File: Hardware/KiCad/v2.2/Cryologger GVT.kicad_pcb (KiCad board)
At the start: 2 copper layers, 144.1 x 96.5 mm, 14 parts, among them J1 Screw_Terminal_01x02, U1 SparkFun_MMDLCB, U2 SparkFun_ZED-F9P, U3 Pololu_D36V6x

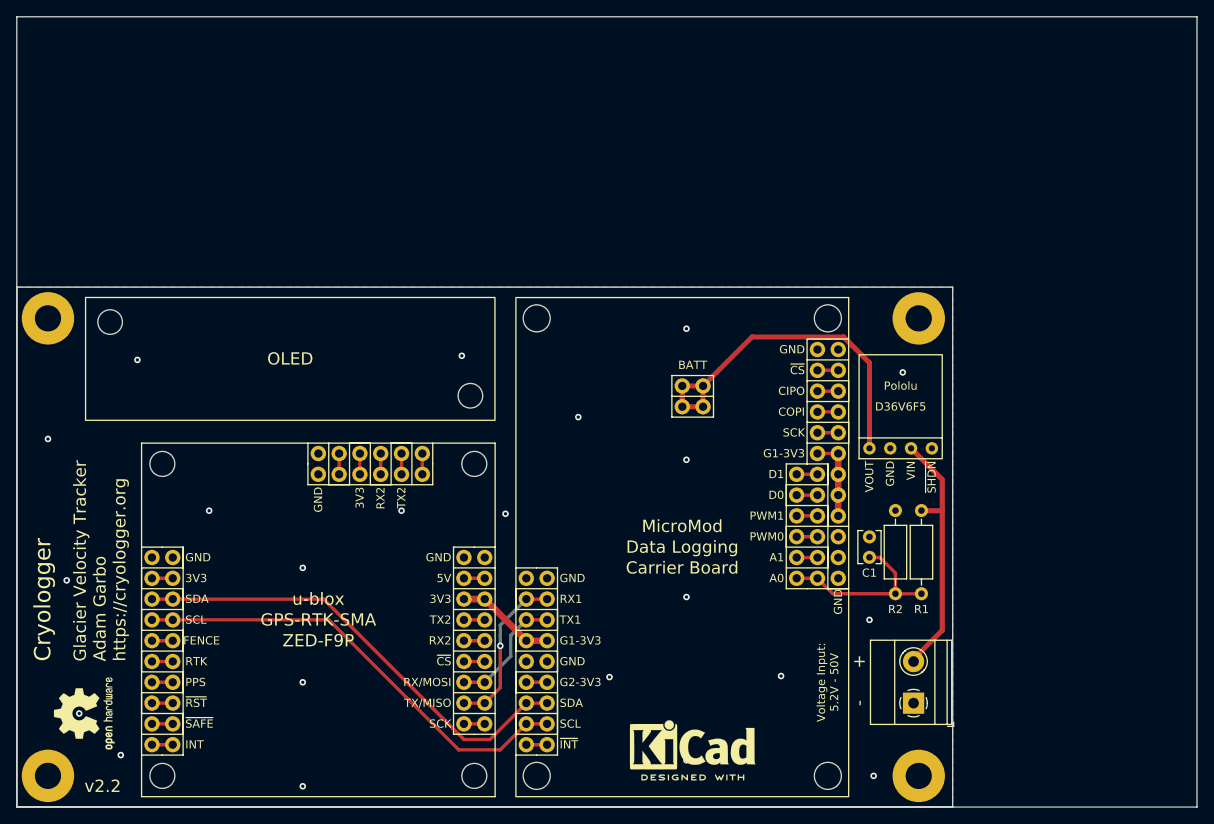
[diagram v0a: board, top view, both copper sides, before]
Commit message: Fix orientation of PCB OLED mounting holes
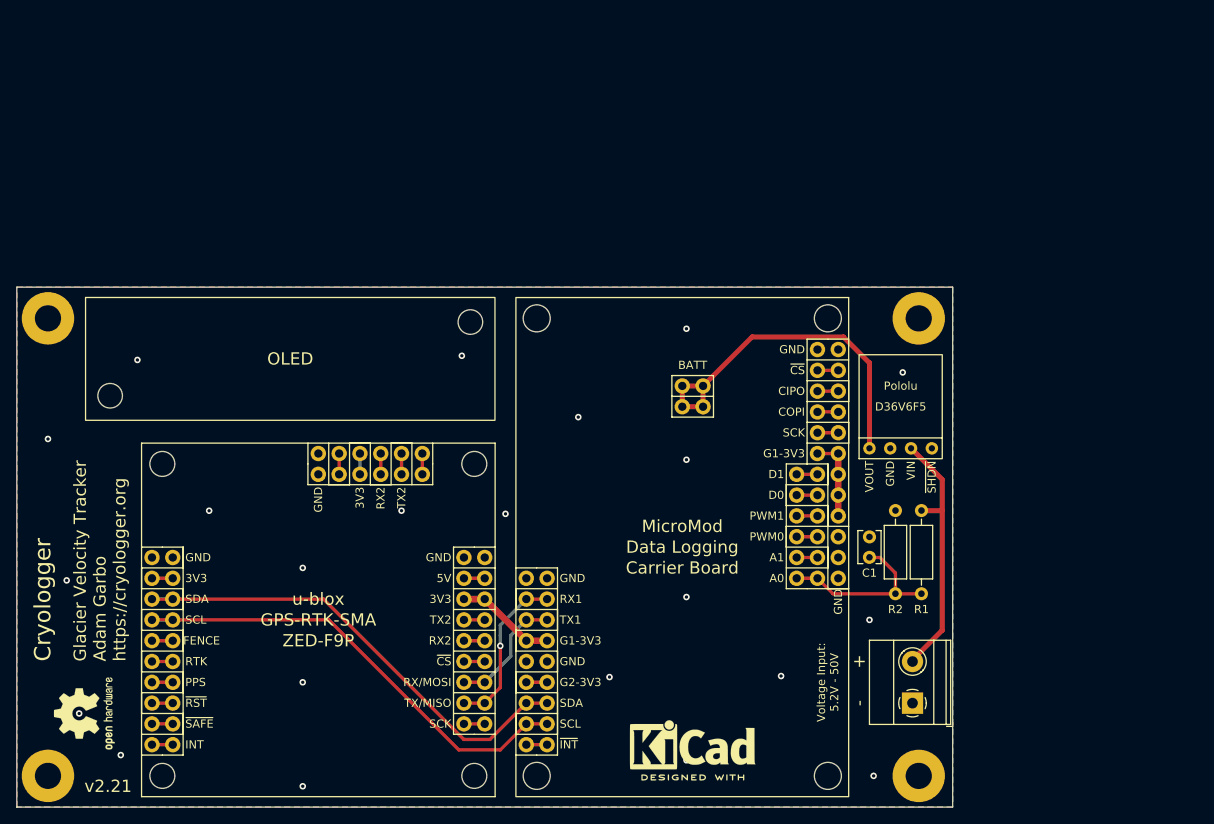
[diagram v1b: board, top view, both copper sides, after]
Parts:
- moved J1 0.13 mm to (200.8, 113.0)
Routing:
- net SDA: track 57.2 -> 59.7 mm
- net SCL: track 56.2 -> 58.7 mm
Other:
- board size 144.1 x 96.5 mm -> 114.3 x 63.5 mm
- board text added: "v2.21"
- board text removed: "v2.2"
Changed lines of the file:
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@@
     )
   )
-  (footprint "Cryologger:SparkFun_OLED" locked (layer "F.Cu")
+  (footprint "Cryologger:SparkFun_OLED" (layer "F.Cu")
     (at 124.841 70.993)
     (attr through_hole)
@@
       (effects (font (size 1 1) (thickness 0.15)))
     )
-    (fp_text value "SparkFun_OLED" (at 0 8.85 unlocked) (layer "F.Fab")
+    (fp_text value "SparkFun_OLED" (at 0 8.85 unlocked) (layer "F.Fab") hide
       (effects (font (size 1 1) (thickness 0.15)))
     )
+    (fp_text user "SparkFun OLED" (at 0 0 unlocked) (layer "F.SilkS") hide
+      (effects (font (size 1.5 1.5) (thickness 0.3)))
+    )
     (fp_text user "OLED" (at 0 0 unlocked) (layer "F.SilkS")
       (effects (font (size 1.5 1.5) (thickness 0.3)))
@@
     )
     (fp_rect (start -25 -7.5) (end 25 7.5) (layer "F.SilkS") (width 0.12) (fill none))
-    (pad "" np_thru_hole circle locked (at 22 4.5) (size 3 3) (drill 3) (layers F&B.Cu *.Mask))
-    (pad "" np_thru_hole circle locked (at -22 -4.5) (size 3 3) (drill 3) (layers F&B.Cu *.Mask))
+    (pad "" np_thru_hole circle (at 22 -4.5) (size 3 3) (drill 3) (layers F&B.Cu *.Mask))
+    (pad "" np_thru_hole circle (at -22 4.5) (size 3 3) (drill 3) (layers F&B.Cu *.Mask))
   )
   (footprint "MountingHole:MountingHole_3.2mm_M3_Pad" (layer "F.Cu")
@@
   )
   (footprint "TerminalBlock_Phoenix:TerminalBlock_Phoenix_MKDS-1,5-2-5.08_1x02_P5.08mm_Horizontal" (layer "F.Cu")
-    (at 200.965003 113.035004 90)
+    (at 200.838 113.035004 90)
     (descr "Terminal Block Phoenix MKDS-1,5-2-5.08, 2 pins, pitch 5.08mm, size 10.2x9.8mm^2, drill diamater 1.3mm, pad diameter 2.6mm, see http://www.farnell.com/datasheets/100425.pdf, script-generated using https://github.com/pointhi/kicad-footprint-generator/scripts/TerminalBlock_Phoenix")
     (tags "THT Terminal Block Phoenix MKDS-1,5-2-5.08 pitch 5.08mm size 10.2x9.8mm^2 drill 1.3mm pad 2.6mm")
@@
   )
   (gr_rect (start 113.03 99.695) (end 143.51 122.555) (layer "B.SilkS") (width 0.15) (fill solid))
-  (gr_rect (start 91.44 125.73) (end 235.585 29.21) (layer "Edge.Cuts") (width 0.1) (fill none))
   (gr_rect (start 91.44 62.23) (end 205.74 125.73) (layer "Edge.Cuts") (width 0.1) (fill none))
   (gr_text "Notes:" (at 140.335 97.79) (layer "B.SilkS")
@@
     (effects (font (size 1.5 1.5) (thickness 0.3)))
   )
-  (gr_text "v2.2" (at 99.695 123.19) (layer "F.SilkS")
+  (gr_text "v2.21" (at 99.695 123.19) (layer "F.SilkS")
     (effects (font (size 1.5 1.5) (thickness 0.3)) (justify left))
   )
@@
     (pts (xy 91.44 125.73) (xy 91.44 62.23))
     (height -3.81)
-    (gr_text "2.5000 in" (at 86.48 93.98 90) (layer "Dwgs.User")
+    (gr_text "2500.0000 mils" (at 86.48 93.98 90) (layer "Dwgs.User")
       (effects (font (size 1 1) (thickness 0.15)))
     )
@@
     (pts (xy 91.44 125.73) (xy 205.74 125.73))
     (height 3.81)
-    (gr_text "4.5000 in" (at 148.59 128.39) (layer "Dwgs.User")
+    (gr_text "4500.0000 mils" (at 148.59 128.39) (layer "Dwgs.User")
       (effects (font (size 1 1) (thickness 0.15)))
     )
@@
     (style (thickness 0.15) (arrow_length 1.27) (text_position_mode 0) (extension_height 0.58642) (extension_offset 0.5) keep_text_aligned)
   )
-  (dimension (type aligned) (layer "Edge.Cuts")
-    (pts (xy 235.585 125.73) (xy 235.585 29.21))
-    (height 5.08)
-    (gr_text "3.8000 in" (at 239.515 77.47 90) (layer "Edge.Cuts")
-      (effects (font (size 1 1) (thickness 0.15)))
-    )
-    (format (units 3) (units_format 1) (precision 4))
-    (style (thickness 0.1) (arrow_length 1.27) (text_position_mode 0) (extension_height 0.58642) (extension_offset 0.5) keep_text_aligned)
-  )
-  (dimension (type aligned) (layer "Edge.Cuts")
-    (pts (xy 91.44 29.21) (xy 235.585 29.21))
-    (height -4.445)
-    (gr_text "5.6750 in" (at 163.5125 23.615) (layer "Edge.Cuts")
-      (effects (font (size 1 1) (thickness 0.15)))
-    )
-    (format (units 3) (units_format 1) (precision 4))
-    (style (thickness 0.1) (arrow_length 1.27) (text_position_mode 0) (extension_height 0.58642) (extension_offset 0.5) keep_text_aligned)
-  )
   (segment (start 189.23 97.79) (end 191.115 99.675) (width 0.4064) (layer "F.Cu") (net 1))
   (segment (start 189.23 97.79) (end 186.69 97.79) (width 0.4064) (layer "F.Cu") (net 1))
@@
   (segment (start 151.765 104.775) (end 153.67 102.87) (width 0.4064) (layer "B.Cu") (net 5))
   (segment (start 151.765 107.315) (end 151.765 104.775) (width 0.4064) (layer "B.Cu") (net 5))
-  (segment (start 148.59 100.33) (end 146.05 100.33) (width 0.8128) (layer "F.Cu") (net 6))
+  (segment (start 146.05 100.33) (end 148.59 100.33) (width 0.8128) (layer "F.Cu") (net 6))
   (segment (start 107.95 97.79) (end 110.49 97.79) (width 0.4064) (layer "F.Cu") (net 6))
-  (segment (start 133.35 85.09) (end 133.35 82.55) (width 0.4064) (layer "F.Cu") (net 6))
   (segment (start 153.67 105.41) (end 156.21 105.41) (width 0.8128) (layer "F.Cu") (net 6))
   (segment (start 191.77 82.55) (end 191.77 90.17) (width 0.8128) (layer "F.Cu") (net 6))
   (segment (start 148.59 100.33) (end 153.67 105.41) (width 0.8128) (layer "F.Cu") (net 6))
   (segment (start 189.23 82.55) (end 191.77 82.55) (width 0.4064) (layer "F.Cu") (net 6))
+  (segment (start 133.35 82.55) (end 133.35 85.09) (width 0.4064) (layer "B.Cu") (net 6))
   (segment (start 153.67 110.49) (end 156.21 110.49) (width 0.4064) (layer "F.Cu") (net 8))
   (segment (start 149.225 117.475) (end 153.67 113.03) (width 0.4064) (layer "F.Cu") (net 9))
@@
   (segment (start 128.905 100.33) (end 146.05 117.475) (width 0.4064) (layer "F.Cu") (net 9))
   (segment (start 146.05 117.475) (end 149.225 117.475) (width 0.4064) (layer "F.Cu") (net 9))
+  (segment (start 107.95 100.33) (end 110.49 100.33) (width 0.4064) (layer "B.Cu") (net 9))
   (segment (start 153.67 115.57) (end 150.495 118.745) (width 0.4064) (layer "F.Cu") (net 10))
   (segment (start 150.495 118.745) (end 145.415 118.745) (width 0.4064) (layer "F.Cu") (net 10))
@@
   (segment (start 153.67 115.57) (end 156.21 115.57) (width 0.4064) (layer "F.Cu") (net 10))
   (segment (start 145.415 118.745) (end 129.54 102.87) (width 0.4064) (layer "F.Cu") (net 10))
+  (segment (start 107.95 102.87) (end 110.49 102.87) (width 0.4064) (layer "B.Cu") (net 10))
   (segment (start 153.67 118.11) (end 156.21 118.11) (width 0.4064) (layer "F.Cu") (net 11))
   (segment (start 189.23 72.39) (end 191.77 72.39) (width 0.4064) (layer "F.Cu") (net 12))
@@
   (segment (start 186.69 95.25) (end 189.23 95.25) (width 0.4064) (layer "F.Cu") (net 20))
   (segment (start 172.72 74.295) (end 172.72 76.835) (width 0.6096) (layer "F.Cu") (net 21))
-  (segment (start 172.72 76.835) (end 175.26 76.835) (width 0.6096) (layer "F.Cu") (net 21))
   (segment (start 192.410256 68.304289) (end 195.58 71.474033) (width 0.6096) (layer "F.Cu") (net 21))
+  (segment (start 172.72 76.835) (end 175.26 76.835) (width 0.6096) (layer "F.Cu") (net 21))
   (segment (start 175.26 74.295) (end 175.26 77.47) (width 0.6096) (layer "F.Cu") (net 21))
   (segment (start 175.26 74.295) (end 172.72 74.295) (width 0.6096) (layer "F.Cu") (net 21))
